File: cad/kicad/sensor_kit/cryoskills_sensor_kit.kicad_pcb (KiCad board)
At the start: 2 copper layers, 120 x 60 mm, 79 parts, among them J1 PWR_In, J10 QWIIC_I2C_2, J11 DS18B20, J12 SERIAL_BREAKOUT, J13 USB_B, J2 PWR_SENSE_Panel, J3 PWR_SENSE_Battery, J4 Adalogger_3V3, J5 Adalogger_VBUS, J6 Adalogger_RegulatorEN, J7 PT1000_RTD_WHEAT, J8 SPI_BREAKOUT, J9 QWIIC_I2C_1, SW1 SPDT Switch, SW2 SW_Push, U1 RFM96W, U2 INA3221, U3 TPS62932DRLR, U4 FT231XQ

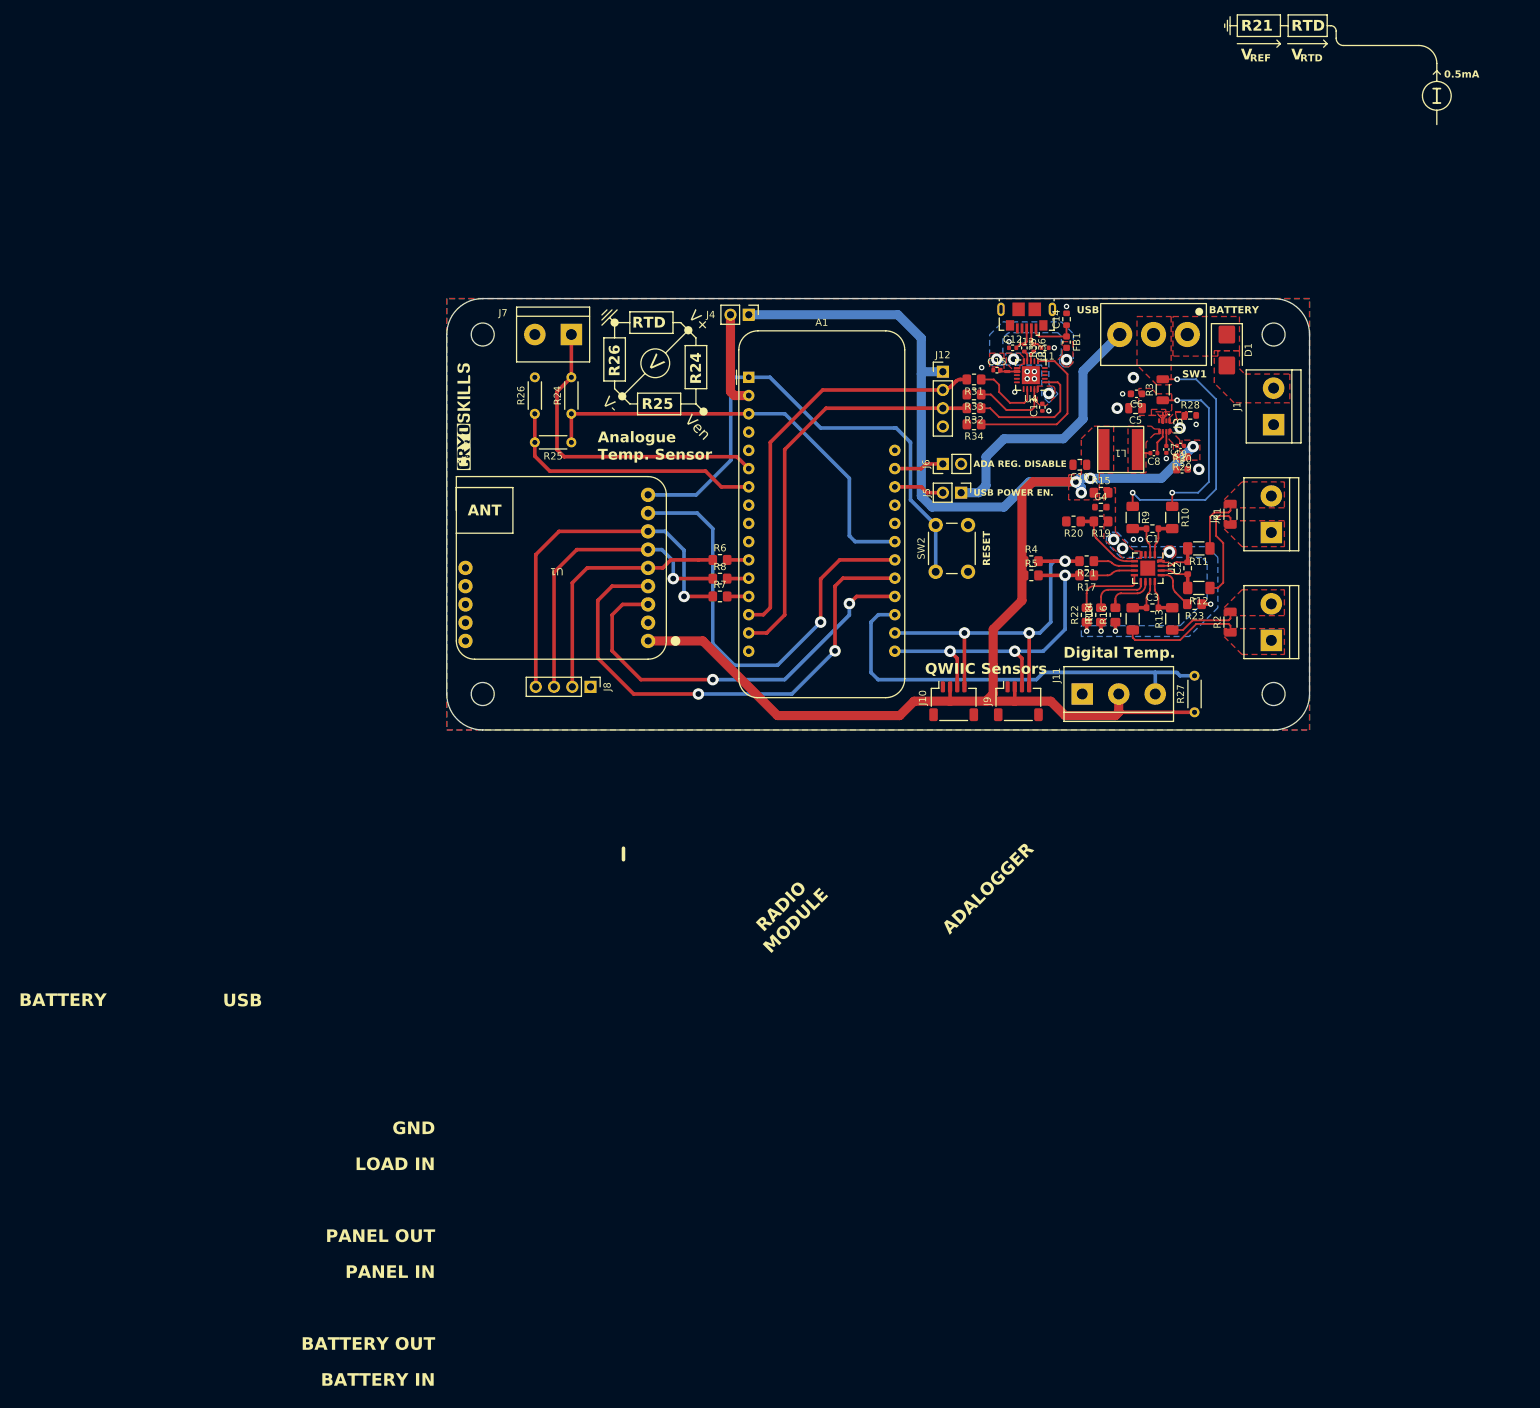
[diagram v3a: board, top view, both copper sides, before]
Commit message: fixes MISO/MOSI on RFM96, swaps Dp/Dm on USB and makes pads for THT resistors bigger
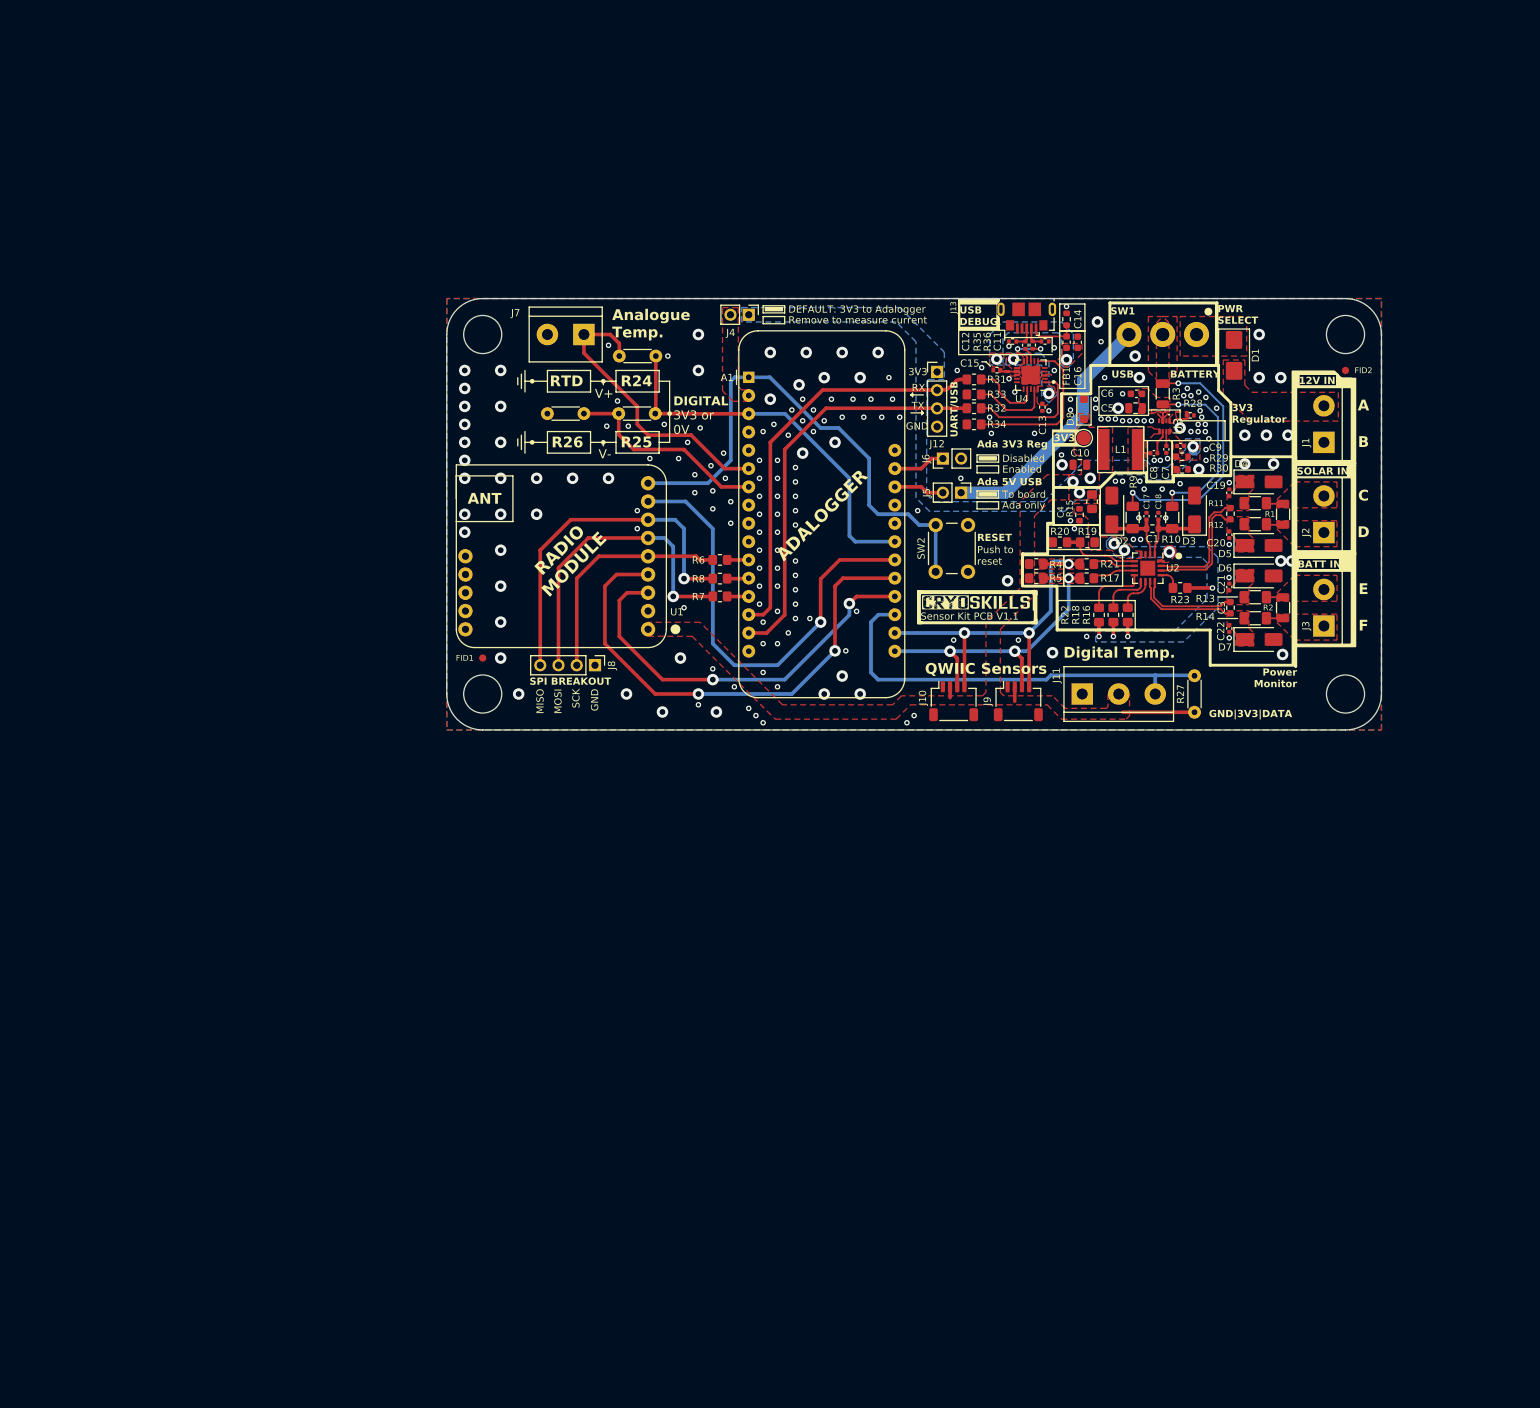
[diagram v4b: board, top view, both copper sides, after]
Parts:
- removed G***: LOGO, LOGO
- added C16: 4.7uF, Capacitor_SMD:C_0603_1608Metric, F.Cu at (146.2, 78.1)
- added C17: 100nF, Capacitor_SMD:C_0402_1005Metric, F.Cu at (155.8, 102.3)
- added C18: 100nF, Capacitor_SMD:C_0402_1005Metric, F.Cu at (157.5, 102.3)
- added C19: 100nF, Capacitor_SMD:C_0402_1005Metric, F.Cu at (167.3, 99.0)
- added C20: 100nF, Capacitor_SMD:C_0402_1005Metric, F.Cu at (167.3, 104.8)
- added C21: 100nF, Capacitor_SMD:C_0402_1005Metric, F.Cu at (167.3, 112.1)
- added C22: 100nF, Capacitor_SMD:C_0402_1005Metric, F.Cu at (167.3, 117.9)
- added D2: SMAJ16A-13-F, Diode_SMD:D_SMA, F.Cu at (151.0, 101.4)
- added D3: SMAJ16A-13-F, Diode_SMD:D_SMA, F.Cu at (162.5, 101.4)
- added D4: SMAJ16A-13-F, Diode_SMD:D_SMA, F.Cu at (171.5, 97.5)
- added D5: SMAJ16A-13-F, Diode_SMD:D_SMA, F.Cu at (171.5, 106.3)
- added D6: SMAJ16A-13-F, Diode_SMD:D_SMA, F.Cu at (171.5, 110.6)
- added D7: SMAJ16A-13-F, Diode_SMD:D_SMA, F.Cu at (171.5, 119.4)
- added D8: NZH3V6B,115, Diode_SMD:D_SOD-123F, F.Cu at (147.1, 87.4)
- added FID1: Fiducial, Fiducial:Fiducial_1mm_Mask2mm, F.Cu at (63.5, 122.0)
- added FID2: Fiducial, Fiducial:Fiducial_1mm_Mask2mm, F.Cu at (183.5, 82.0)
- added TP1: 3V3, TestPoint:TestPoint_Pad_D2.0mm, F.Cu at (147.1, 91.4)
- C10: value 100nF -> 22uF
- H1, H2, H3, H4: footprint MountingHole:MountingHole_3.2mm_M3 -> MountingHole:MountingHole_5.3mm_M5
- R28: footprint Resistor_SMD:R_0603_1608Metric -> Resistor_SMD:R_0402_1005Metric
- R29, R30: footprint Capacitor_SMD:C_0603_1608Metric -> Resistor_SMD:R_0603_1608Metric
- moved R14 17.1 mm to (170.9, 116.5), turned to 180 degrees
- moved R24 14.2 mm to (87.6, 80.0), turned to 180 degrees
- moved R25 12.3 mm to (87.5, 88.0)
- moved R13 11.9 mm to (170.9, 113.5), turned to 180 degrees
- moved R12 11.8 mm to (170.9, 103.4)
- moved C3 10.8 mm to (167.5, 115.0), turned to 90 degrees
- moved R11 10.1 mm to (170.9, 100.5)
- moved H1 10.0 mm to (183.5, 77.0)
- moved H2 10.0 mm to (183.5, 127.0)
- moved C2 9.64 mm to (167.5, 101.9)
- moved J3 7.59 mm to (180.5, 117.5)
- moved R2 7.59 mm to (174.8, 115.0)
- moved J1 7.42 mm to (180.5, 92.0)
- moved J2 7.32 mm to (180.5, 104.5)
- moved R1 7.32 mm to (174.8, 102.0)
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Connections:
- net /Power Monitor/INA3221_INm1 renamed /Power Monitor/INA3221_IN1-
- net /Power Monitor/INA3221_INm2 renamed /Power Monitor/INA3221_IN2-
- net /Power Monitor/INA3221_INm3 renamed /Power Monitor/INA3221_IN3-
- net /Power Monitor/INA3221_INp1 renamed /Power Monitor/INA3221_IN1+
- net /Power Monitor/INA3221_INp2 renamed /Power Monitor/INA3221_IN2+
- net /Power Monitor/INA3221_INp3 renamed /Power Monitor/INA3221_IN3+
- R35 pad 2: Net-(U4-USBDM) -> Net-(U4-USBDP)
- R36 pad 2: Net-(U4-USBDP) -> Net-(U4-USBDM)
- U1 pad 6: /MOSI -> /MISO
- U1 pad 7: /MISO -> /MOSI
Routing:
- net /VCC_3V3: track 224.3 -> 14.1 mm
- net /Isense_Battery_B: track 16.8 -> 2.32 mm
- net /VCC_3V3_Adalogger: track 13.5 -> 0.00 mm
- net /Isense_Panel_B: track 14.6 -> 2.35 mm
- net /Power Monitor/INA3221_IN2-: track 5.74 -> 16.7 mm
- net /Power Monitor/INA3221_IN2+: track 5.74 -> 16.7 mm
- net /Power Monitor/INA3221_IN1-: track 5.69 -> 14.3 mm
- net /ADC_RTDm: track 37.4 -> 28.9 mm
- net /Power Monitor/INA3221_IN1+: track 5.69 -> 13.7 mm
- net /Isense_Battery_A: track 9.73 -> 2.32 mm
- net /ADC_REF+: track 60.5 -> 53.4 mm
- net /Isense_Panel_A: track 8.56 -> 2.35 mm
- net Net-(U4-USBDM): track 1.51 -> 6.97 mm, vias 0 -> 2
- net /Power Monitor/VCC_INA3221: track 5.00 -> 9.50 mm
- net /Power Monitor/INA3221_IN3-: track 5.69 -> 10.0 mm
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- added copper zone on F.Cu, net /Power Monitor/INA3221_IN1+
- added copper zone on F.Cu, net /Power Monitor/INA3221_IN1-
- added copper zone on F.Cu, net /Power Monitor/INA3221_IN2+
- added copper zone on F.Cu, net /Power Monitor/INA3221_IN2-
- added copper zone on F.Cu, net /SCL
- added copper zone on F.Cu, net /SDA
- added copper zone on B.Cu, net /VCC_3V3
- added copper zone on F.Cu, net /VCC_3V3_Adalogger
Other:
- board size 120 x 60 mm -> 130 x 60 mm
- board text added: "12V IN"
- board text added: "3V3"
- board text added: "3V3 Regulator"
- board text added: "3V3 or 0V"
- board text added: "A"
- board text added: "Ada 3V3 Reg"
- board text added: "Ada 5V USB"
- board text added: "Ada only"
- board text added: "Analogue Temp."
- board text added: "B"
- board text added: "BATT IN"
- board text added: "C"
- board text added: "D"
- board text added: "DEFAULT: 3V3 to Adalogger"
- board text added: "DIGITAL"
- board text added: "Disabled"
- board text added: "E"
- board text added: "Enabled"
- board text added: "F"
- board text added: "GND|3V3|DATA"
- board text added: "MISO"
- board text added: "MOSI"
- board text added: "PWR SELECT"
- board text added: "Power Monitor"
- board text added: "Push to reset"
- board text added: "RX"
- board text added: "Remove to measure current"
- board text added: "SCK"
- board text added: "SOLAR IN"
- board text added: "SPI BREAKOUT"
- board text added: "Sensor Kit PCB V1.1"
- board text added: "TX"
- board text added: "To board"
- board text added: "UART/USB"
- board text added: "USB DEBUG"
- board text removed: "0.5mA"
- board text removed: "ADA REG. DISABLE"
- board text removed: "Analogue Temp. Sensor"
- board text removed: "BATTERY IN"
- board text removed: "BATTERY OUT"
- board text removed: "LOAD IN"
- board text removed: "PANEL IN"
- board text removed: "PANEL OUT"
- board text removed: "R21"
- board text removed: "REF"
- board text removed: "USB POWER EN."
- board text removed: "V"
- board text removed: "Ven"
